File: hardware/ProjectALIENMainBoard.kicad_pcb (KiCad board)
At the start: 2 copper layers, 69.1 x 100.6 mm, 53 parts, among them J1 Bumper, J10 Excess GPIO Pins, J3 Left Motor, J4 Right Motor, J5 Pixels, J6 Ultrasonic, J7 Micro USB, J8 I2C Multiplexer, J9 Voltage Breakout, Q1 2N3904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

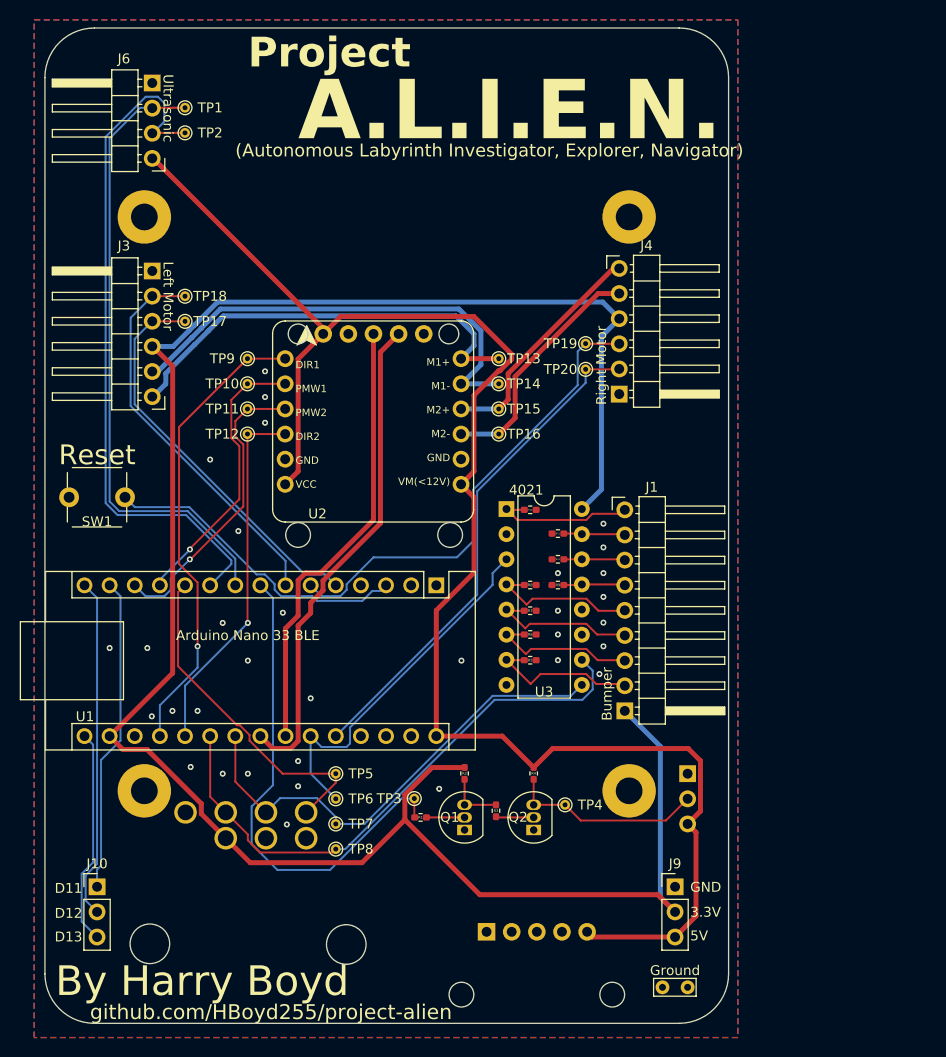
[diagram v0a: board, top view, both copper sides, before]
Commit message: Tidied up traces
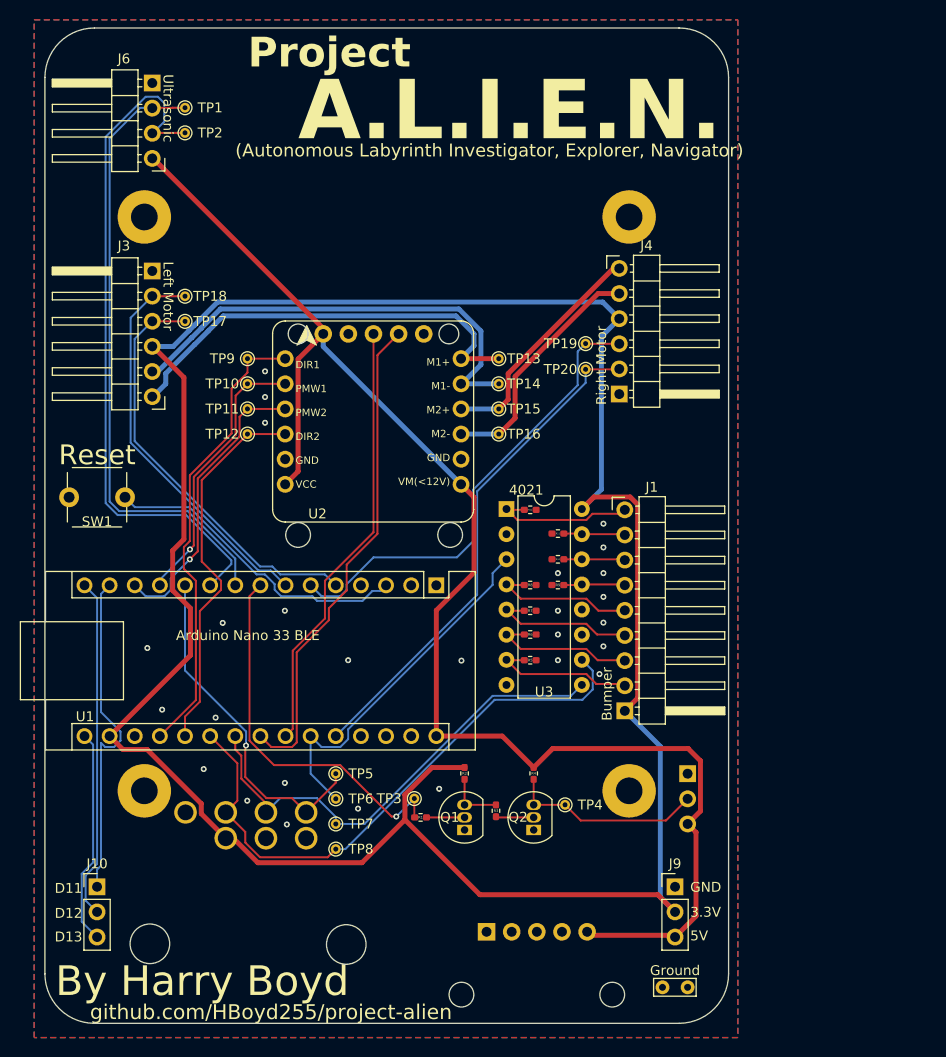
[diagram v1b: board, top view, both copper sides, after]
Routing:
- net +3.3V: track 214.2 -> 244.5 mm
- net +5V: track 164.1 -> 148.3 mm
- net PIXELS_DATA_3.3V: track 50.0 -> 38.7 mm, vias 0 -> 1
- net ENC1A: track 40.3 -> 42.5 mm
- net D11: track 31.9 -> 34.0 mm
- net SHIFT_REG_CLOCK: track 57.8 -> 59.4 mm
- net DIR2: track 37.0 -> 38.6 mm, vias 1 -> 0
- net I2C_SCL: track 45.2 -> 44.3 mm
- net Net-(J1-Pin_2): track 15.7 -> 14.9 mm
- net ENC1B: track 39.9 -> 40.7 mm
- net PWM2: track 30.4 -> 29.7 mm
- net PWM1: track 28.6 -> 27.9 mm
- net DIR1: track 47.2 -> 46.6 mm, vias 1 -> 0
- net NES_DATA: track 34.4 -> 34.8 mm, vias 0 -> 1
- net GND: vias 33 -> 27

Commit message: Flipped and repositioned motor connectors
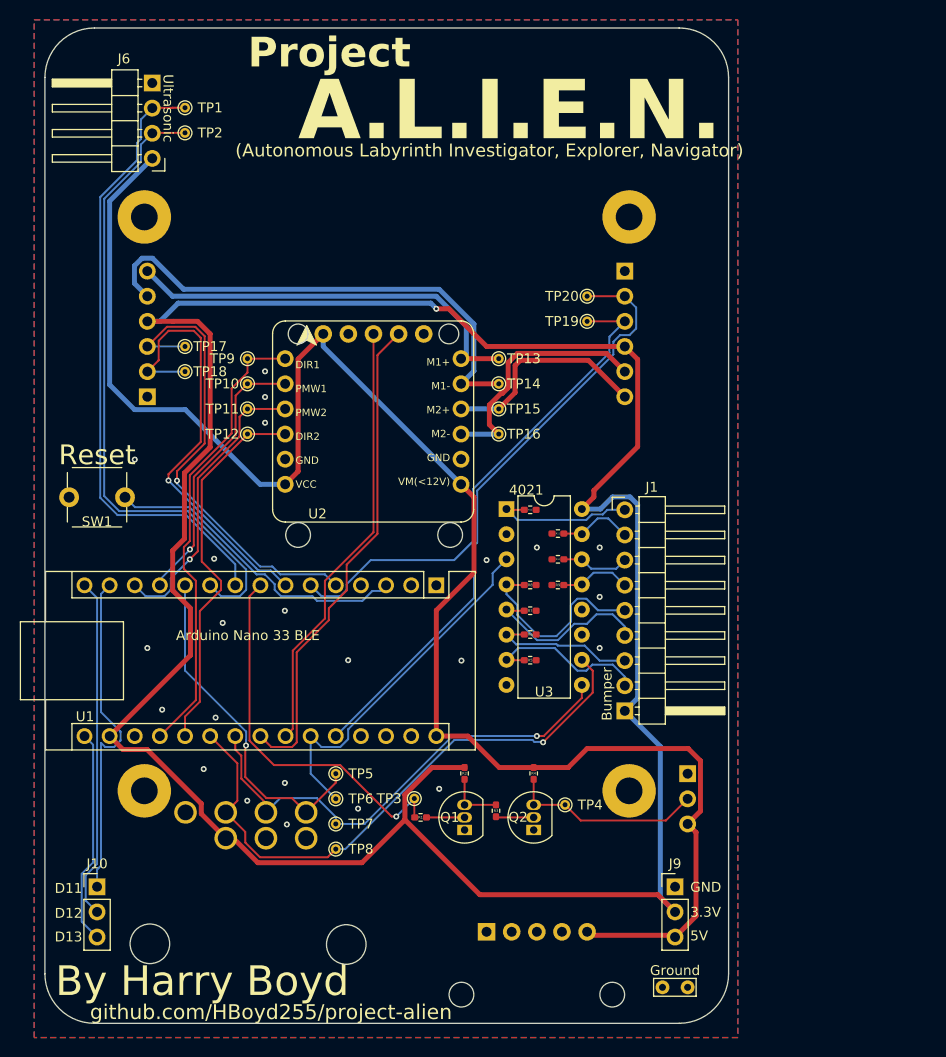
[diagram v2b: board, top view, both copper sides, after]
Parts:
- J3, J4: moved to B.Cu
- moved J4 13.0 mm to (162.6, 90.2)
- moved J3 12.7 mm to (114.3, 77.5)
- moved TP18 7.62 mm to (118.1, 87.6)
- moved TP20 7.39 mm to (158.8, 80.0)
- moved TP17 2.54 mm to (118.1, 85.1)
- moved TP19 2.25 mm to (158.8, 82.5)
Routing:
- net +5V: track 148.3 -> 170.6 mm
- net ENC2B: track 50.9 -> 61.9 mm
- net +3.3V: track 244.5 -> 252.1 mm, vias 0 -> 1
- net Net-(J1-Pin_5): track 14.9 -> 20.2 mm
- net ENC1A: track 42.5 -> 47.2 mm, vias 0 -> 1
- net M1-: track 46.8 -> 51.4 mm
- net USONIC_TRIG: track 70.1 -> 65.8 mm
- net ENC2A: track 47.6 -> 51.9 mm
- net ENC1B: track 40.7 -> 44.4 mm, vias 0 -> 1
- net Net-(J1-Pin_4): track 14.9 -> 18.3 mm
- net M1+: track 44.1 -> 41.9 mm
- net Net-(J1-Pin_2): track 14.9 -> 16.9 mm
- net M2+: track 23.4 -> 21.7 mm
- net Net-(J1-Pin_8): track 6.22 -> 7.54 mm
- net Net-(J1-Pin_6): track 6.22 -> 7.21 mm
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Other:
- board text added: "Project A.L.I.E.N. Main Board V1.2 06/09/2024 Harry Boyd"
- board text removed: "Project A.L.I.E.N. Main Board V1.1 24/08/2024 Harry Boyd"
